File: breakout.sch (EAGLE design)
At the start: 38 parts, among them J2 1x3 RA Female .1", J3 CORTEX_DEBUG_PTH

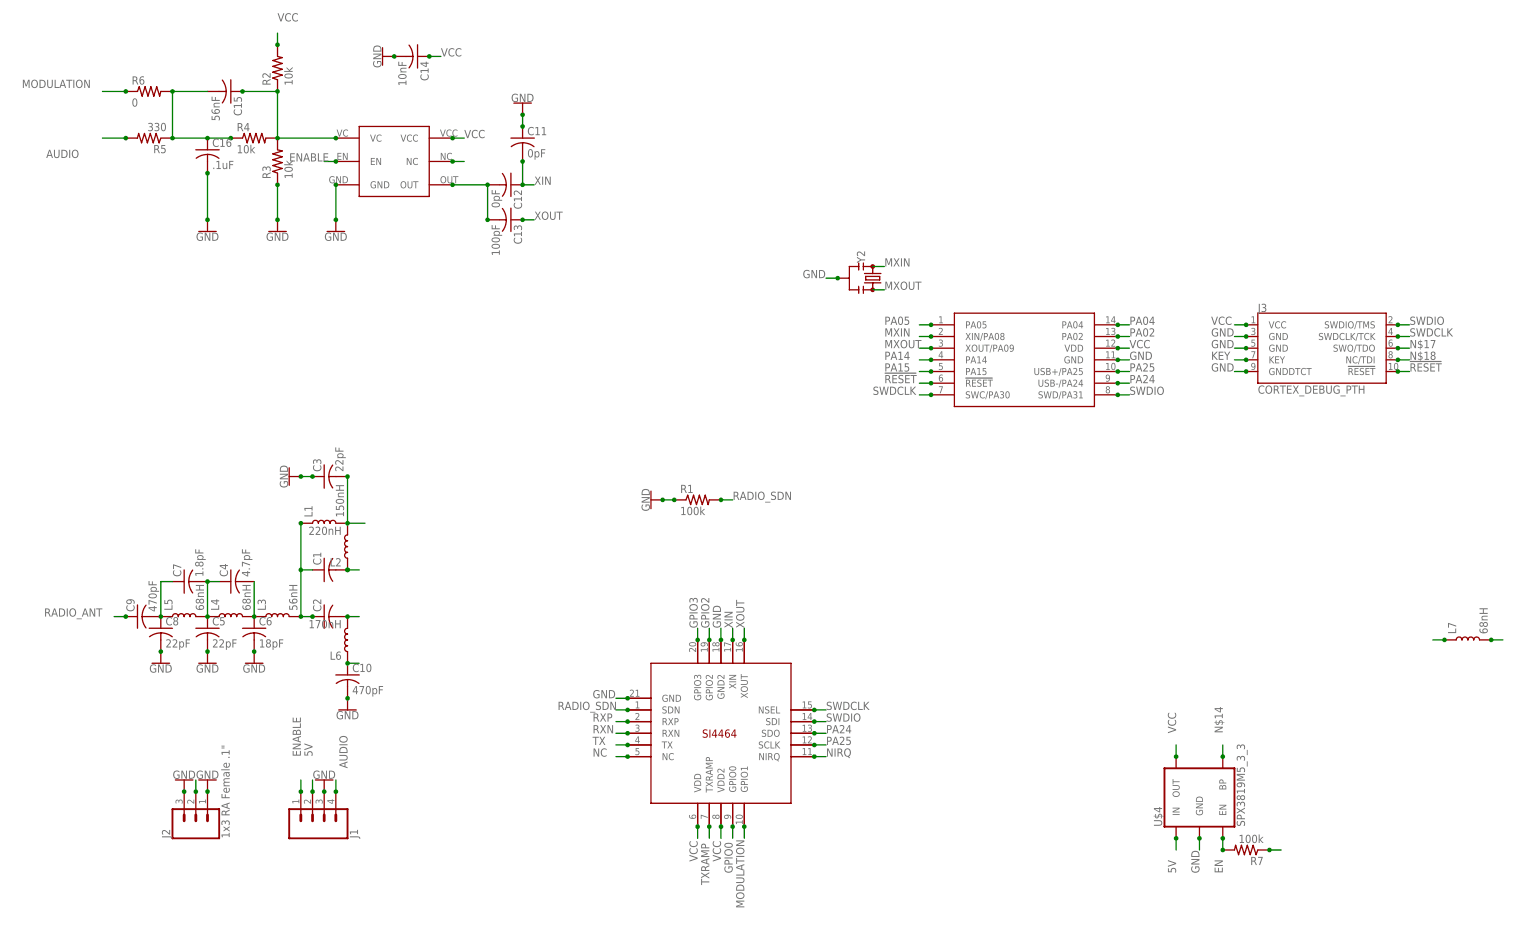
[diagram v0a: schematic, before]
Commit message: Added SAMD11C14
second routing pass, moved to SAMD11C14 ARM processor
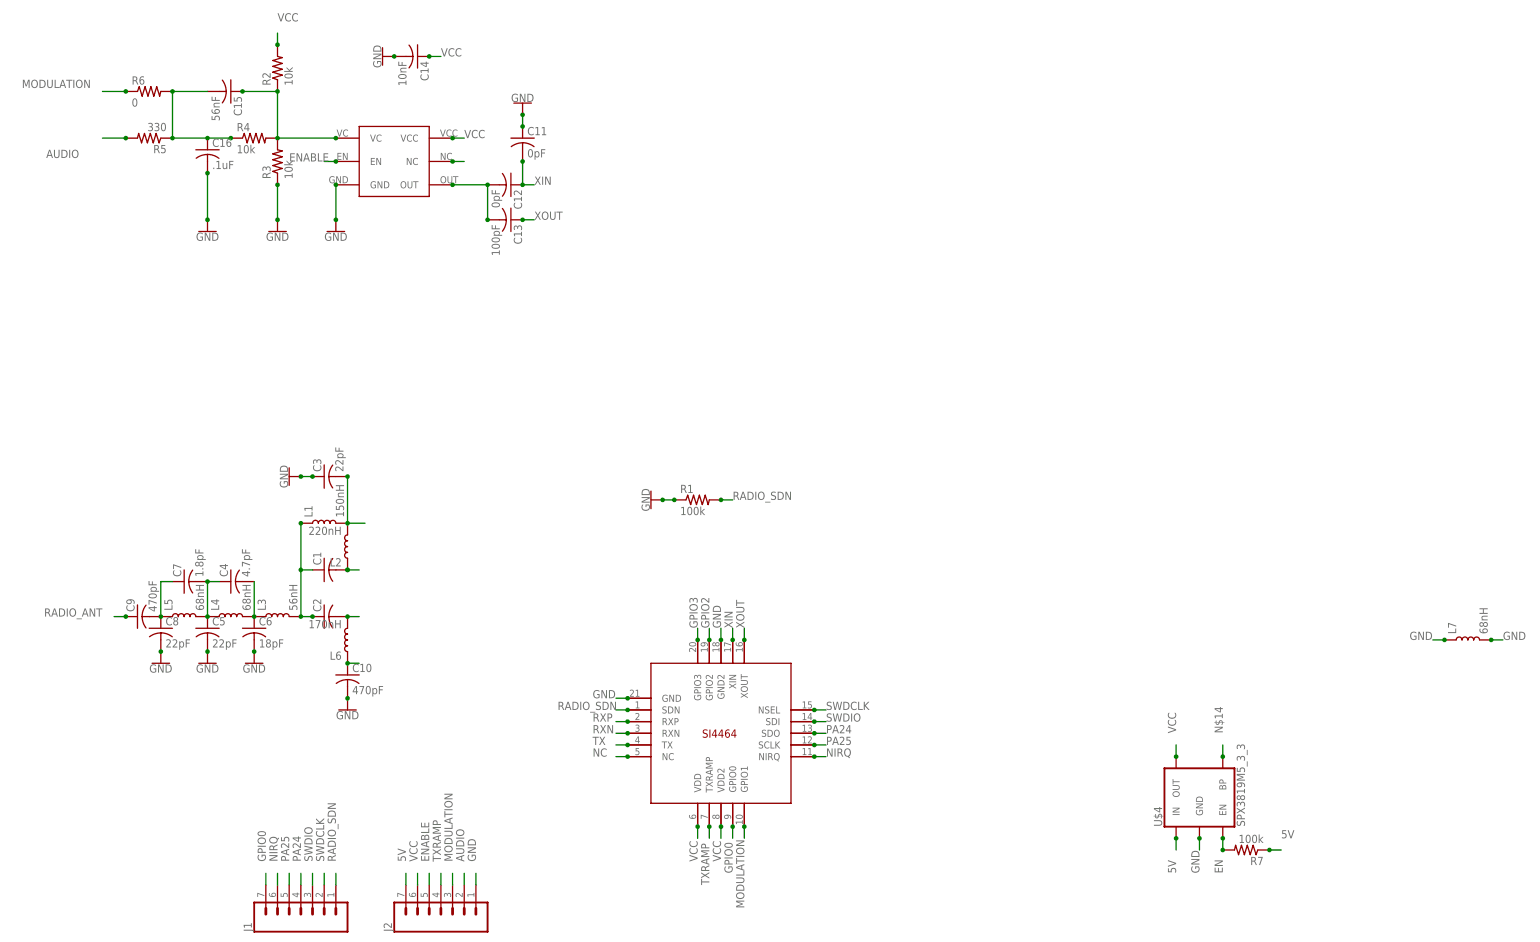
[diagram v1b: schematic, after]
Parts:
- removed J3: CORTEX_DEBUG_PTH, SparkFun-Connectors:CORTEX_DEBUG_PTH
- removed U$3: SAMD11C14, atmel_tiny24-44-84tiny48-88mega48-88-168-328:SAMD11C14
- removed Y2: (no value), SparkFun-Clocks:RESONATORSMD-3.2X1.3
- J1: device SparkFun-Connectors:CONN_04SMD_RA_FEMALE -> SparkFun-Connectors:CONN_07
- J2: value 1x3 RA Female .1" -> (none); device SparkFun-Connectors:CONN_03SMD_RA_FEMALE -> SparkFun-Connectors:CONN_07
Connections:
- removed net !RESET: J3.!RESET, U$3.!RESET
- removed net KEY: J3.KEY
- removed net MXIN: U$3.XIN/PA08, Y2.1
- removed net MXOUT: U$3.XOUT/PA09, Y2.3
- removed net N$17: J3.SWO/TDO
- removed net N$18: J3.NC/TDI
- removed net PA02: U$3.PA02
- removed net PA04: U$3.PA04
- removed net PA05: U$3.PA05
- removed net PA14: U$3.PA14
- removed net PA15: U$3.PA15
- net 5V: now also J2.7; no longer J1.2
- net AUDIO: now also J2.2; no longer J1.4
- net ENABLE: now also J2.5; no longer J1.1
- net GND: no longer J1.3, J2.3, J3.GND@3, J3.GND@5, J3.GNDDTCT, U$3.GND, Y2.2
- net GPIO0: now also J1.7
- net MODULATION: now also J2.3
- net NIRQ: now also J1.6
- net PA24: now also J1.4; no longer U$3.USB-/PA24
- net PA25: now also J1.5; no longer U$3.USB+/PA25
- net RADIO_ANT: no longer J2.2
- net RADIO_SDN: now also J1.1
- net SWDCLK: now also J1.2; no longer J3.SWDCLK/TCK, U$3.SWC/PA30
- net SWDIO: now also J1.3; no longer J3.SWDIO/TMS, U$3.SWD/PA31
- net TXRAMP: now also J2.4
- net VCC: now also J2.6; no longer J3.VCC, U$3.VDD
